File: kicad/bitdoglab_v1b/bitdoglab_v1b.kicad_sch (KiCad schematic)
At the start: 35 parts, among them J1 WS2812, J10 Conn_01x05_Pin, J11 Conn_02x05_Counter_Clockwise, J2 conector_idc, J3 JOYSTICK, J4 jumper_mic, J5 Conn_01x05_Pin, J6 Conn_01x05_Pin, J8 Conn_02x05_Counter_Clockwise, J9 Conn_01x05_Pin, Q1 BC337, Q2 BC337, Q3 DMG2305UX-13, SW1 RESET, SW2 Button_A, SW3 Button_B, U1 uA7805, U2 1063, U3 Charger2A

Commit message: Começo da construção do layout
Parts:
- removed J11, J8: Conn_02x05_Counter_Clockwise, symbol Connector_Generic:Conn_02x05_Counter_Clockwise
- added J13: GP03, Connector_Wire:SolderWire-2sqmm_1x02_P7.8mm_D2mm_OD3.9mm, symbol Connector_Generic:Conn_01x01
- added J14: GP02, Connector_Wire:SolderWire-2sqmm_1x02_P7.8mm_D2mm_OD3.9mm, symbol Connector_Generic:Conn_01x01
- added J15: GP01, Connector_Wire:SolderWire-2sqmm_1x02_P7.8mm_D2mm_OD3.9mm, symbol Connector_Generic:Conn_01x01
- added J16: GP00, Connector_Wire:SolderWire-2sqmm_1x02_P7.8mm_D2mm_OD3.9mm, symbol Connector_Generic:Conn_01x01
- added J5: GND, Connector_Wire:SolderWire-2sqmm_1x02_P7.8mm_D2mm_OD3.9mm, symbol Connector_Generic:Conn_01x01
- added J6: GP28, Connector_Wire:SolderWire-2sqmm_1x02_P7.8mm_D2mm_OD3.9mm, symbol Connector_Generic:Conn_01x01
- added J7: AGND, Connector_Wire:SolderWire-2sqmm_1x02_P7.8mm_D2mm_OD3.9mm, symbol Connector_Generic:Conn_01x01
- added J8: 3.3_OUT, Connector_Wire:SolderWire-2sqmm_1x02_P7.8mm_D2mm_OD3.9mm, symbol Connector_Generic:Conn_01x01
- added J9: VBUS, Connector_Wire:SolderWire-2sqmm_1x02_P7.8mm_D2mm_OD3.9mm, symbol Connector_Generic:Conn_01x01
- added U1: 3.3v_tht, Package_TO_SOT_THT:TO-220-3_Vertical, symbol dk_PMIC-Voltage-Regulators-Linear:LD1117V33
- A1: footprint Raspberry_Pi_Pico_W_Kicad_Files-main:MODULE_SC0918 -> user_Raspberry_Pi_Pico_W_Kicad_Files-main:MODULE_SC0918
- BT1: footprint (none) -> Battery:BatteryHolder_MPD_BH-18650-PC2
- BZ2: renamed from BZ3; footprint (none) -> Buzzer_Beeper:MagneticBuzzer_CUI_CMT-8504-100-SMT
- BZ4: footprint (none) -> Buzzer_Beeper:MagneticBuzzer_CUI_CMT-8504-100-SMT
- C1, C2: footprint (none) -> Capacitor_SMD:CP_Elec_5x5.9
- D1: footprint (none) -> LED_SMD:LED_RGB_5050-6
- D2: footprint (none) -> LED_THT:LED_D5.0mm-4_RGB_Wide_Pins
- J1: renamed from J2; footprint (none) -> Connector_PinHeader_2.54mm:PinHeader_2x07_P2.54mm_Vertical
- J10: renamed from J5; footprint (none) -> Connector_PinHeader_2.54mm:PinHeader_1x05_P2.54mm_Vertical
- J11: renamed from J10; footprint (none) -> Connector_PinHeader_2.54mm:PinHeader_1x05_P2.54mm_Vertical
- J12: renamed from J1; value WS2812 -> WS2812 5x5 Matrix led; footprint (none) -> matrix5x5:Ws2812_led_5050_rgb_5x5
- J17: renamed from J3; footprint (none) -> user_ky-023-joystick-module-1.snapshot.4:ky-023
- J2: renamed from J4; footprint (none) -> Connector_PinHeader_2.54mm:PinHeader_1x02_P2.54mm_Vertical
- J3: renamed from J9; footprint (none) -> Connector_PinHeader_2.54mm:PinHeader_1x05_P2.54mm_Vertical
- J4: renamed from J6; footprint (none) -> Connector_PinHeader_2.54mm:PinHeader_1x05_P2.54mm_Vertical
- OLED1: footprint (none) -> user_SSD1306:128x64OLED
- Q1: renamed from Q3; footprint digikey-footprints:SOT-23-3 -> Package_TO_SOT_SMD:SOT-23-3
- Q2: renamed from Q1; footprint Package_TO_SOT_THT:TO-92_Inline -> Package_TO_SOT_THT:TO-92
- Q3: renamed from Q2; footprint Package_TO_SOT_THT:TO-92_Inline -> Package_TO_SOT_THT:TO-92
- R1: renamed from R4; value R -> 330; footprint (none) -> Resistor_THT:R_Axial_DIN0207_L6.3mm_D2.5mm_P7.62mm_Horizontal
- R2: renamed from R1; value R -> 330; footprint (none) -> Resistor_THT:R_Axial_DIN0207_L6.3mm_D2.5mm_P7.62mm_Horizontal
- Rb1: renamed from Rb; footprint (none) -> Resistor_THT:R_Axial_DIN0207_L6.3mm_D2.5mm_P7.62mm_Horizontal
- Rg1: renamed from Rg; footprint (none) -> Resistor_THT:R_Axial_DIN0207_L6.3mm_D2.5mm_P7.62mm_Horizontal
- Rr1: renamed from Rr; footprint (none) -> Resistor_THT:R_Axial_DIN0207_L6.3mm_D2.5mm_P7.62mm_Horizontal
- SW1, SW2, SW3: footprint (none) -> Button_Switch_THT:SW_PUSH_6mm
- U2: renamed from U1; value uA7805 -> 3.3v_smd; footprint (none) -> Package_TO_SOT_SMD:SOT-223
- U3: value Charger2A -> BAT (DIS)CHARGE; footprint (none) -> user_HW775-main:Charger2A
- U4: renamed from U2; footprint MODULE_1063 -> user_SSD1306:128x64OLED
- renumbered BZ2 to BZ3
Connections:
- net +3.3V: now also U1.2
- net 3.3_OUT: no longer J4.3 (Pin_3)
- net GNDREF: now also J5.1 (Pin_1), U1.1; no longer J4.4 (Pin_4)
- net GP0: no longer J11.4 (Pin_4)
- net GP01: no longer J11.3 (Pin_3)
- net GP02: no longer J11.2 (Pin_2)
- net GP03: no longer J11.1 (Pin_1)
- net VBUS: now also U1.3; no longer J4.2 (Pin_2)
- net 5 renamed GP28
- net GP28: no longer J4.5 (Pin_5)
- new net 3.3_OUT_EXT: J4.4 (Pin_4), J8.1 (Pin_1)
- new net AGND_EXT: J4.3 (Pin_3), J7.1 (Pin_1)
- new net GP01_EXT: J11.3 (Pin_3), J15.1 (Pin_1)
- new net GP02_EXT: J11.2 (Pin_2), J14.1 (Pin_1)
- new net GP03_EXT: J11.1 (Pin_1), J13.1 (Pin_1)
- new net GP0_EXT: J11.4 (Pin_4), J16.1 (Pin_1)
- new net GP28_EXT: J4.2 (Pin_2), J6.1 (Pin_1)
- new net VBUS_EXT: J4.5 (Pin_5), J9.1 (Pin_1)
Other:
- moved on the sheet: C1, C2

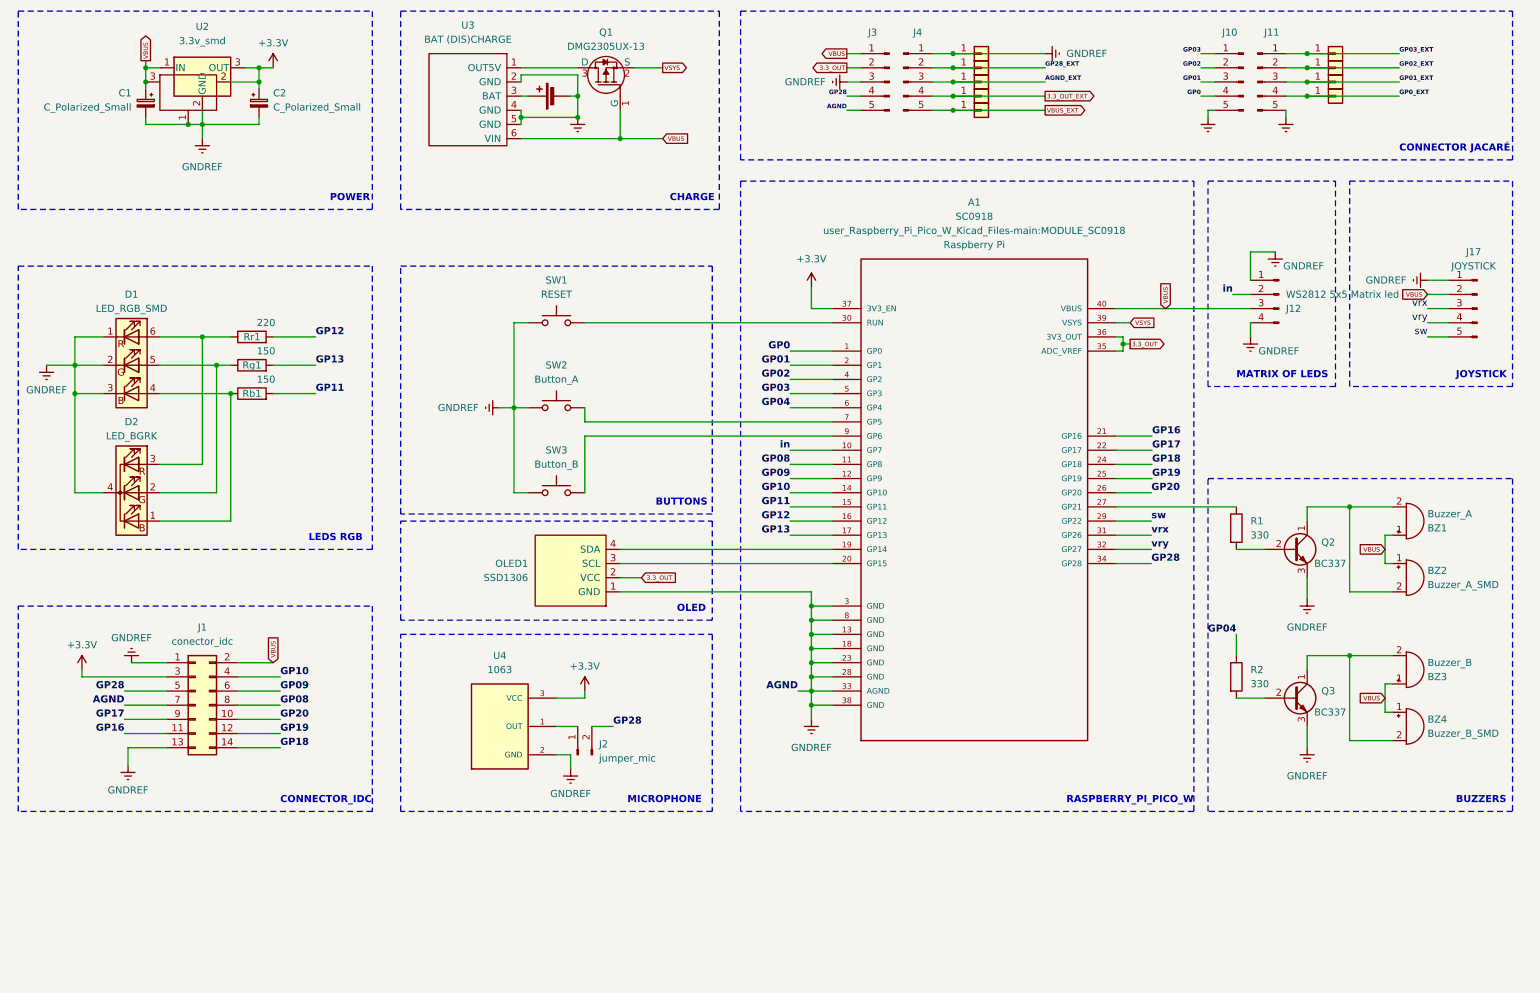
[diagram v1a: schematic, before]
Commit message: Finalizacao do placement dos componentes
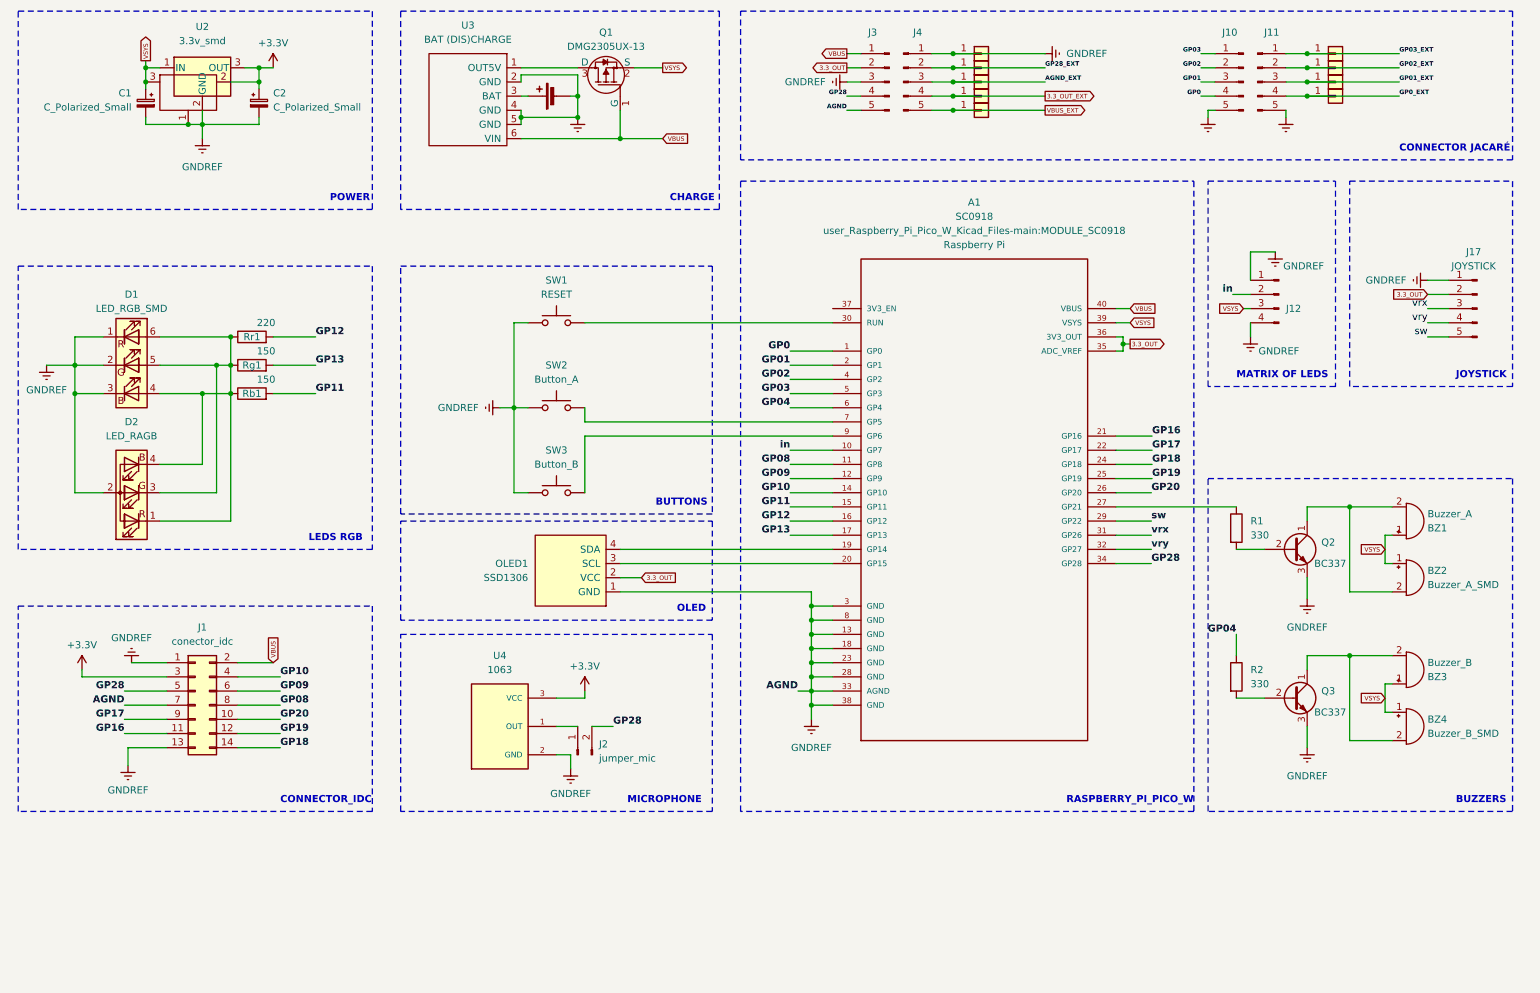
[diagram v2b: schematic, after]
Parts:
- removed D2: LED_BGRK, LED_THT:LED_D5.0mm-4_RGB_Wide_Pins, symbol Device:LED_BGRK
- added D2: LED_RAGB, LED_THT:LED_D5.0mm-4_RGB_Wide_Pins, symbol Device:LED_RAGB
- J12: value WS2812 5x5 Matrix led -> 5x5 Matrix led
- U4: footprint user_SSD1306:128x64OLED -> user_1063:MODULE_1063
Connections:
- net +3.3V: no longer A1.37 (3V3_EN)
- net 3.3_OUT: now also J17.2 (Pin_2)
- net GNDREF: now also SW1.2, SW2.2, SW3.2, D2.2 (A); no longer SW1.1, SW2.1, SW3.1
- net VBUS: no longer BZ1.1 (-), BZ2.1 (-), BZ3.1 (-), BZ4.1 (-), C1.1, J12.3 (Pin_3), J17.2 (Pin_2), U1.3, U2.1 (IN)
- net VSYS: now also BZ1.1 (-), BZ2.1 (-), BZ3.1 (-), BZ4.1 (-), C1.1, J12.3 (Pin_3), U1.3, U2.1 (IN)
- net at D1.5 (GA), Rg1.1: now also D1.4 (BA), D1.6 (RA), Rb1.1, Rr1.1, D2.1 (RK), D2.3 (GK), D2.4 (BK)
- net at A1.30 (RUN): now also SW1.1; no longer SW1.2
- net at A1.7 (GP5): now also SW2.1; no longer SW2.2
- net at A1.9 (GP6): now also SW3.1; no longer SW3.2

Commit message: roteamento e apagando backups
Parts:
- added J1, J3: Conn_01x20_Socket, Connector_PinHeader_2.54mm:PinHeader_1x20_P2.54mm_Vertical, symbol Connector:Conn_01x20_Socket
- renumbered J8 to J10, J9 to J11, J10 to J12, J11 to J13, J12 to J14, J13 to J15, J14 to J16, J15 to J17, J16 to J18, J17 to J19, J1 to J2, J2 to J4, J3 to J5, J4 to J6, J5 to J7, J6 to J8, J7 to J9
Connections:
- net 3.3_OUT: now also J3.15 (Pin_15), J3.16 (Pin_16)
- net GNDREF: now also J1.13 (Pin_13), J1.18 (Pin_18), J1.3 (Pin_3), J1.8 (Pin_8), J3.13 (Pin_13), J3.18 (Pin_18), J3.3 (Pin_3), J3.8 (Pin_8)
- net GP0: now also J1.1 (Pin_1)
- net GP01: now also J1.2 (Pin_2)
- net GP02: now also J1.4 (Pin_4)
- net GP03: now also J1.5 (Pin_5)
- net GP04: now also J1.6 (Pin_6)
- net GP08: now also J1.11 (Pin_11)
- net GP09: now also J1.12 (Pin_12)
- net GP10: now also J1.14 (Pin_14)
- net GP11: now also J1.15 (Pin_15)
- net GP12: now also J1.16 (Pin_16)
- net GP13: now also J1.17 (Pin_17)
- net GP16: now also J3.1 (Pin_1)
- net GP17: now also J3.2 (Pin_2)
- net GP18: now also J3.4 (Pin_4)
- net GP19: now also J3.5 (Pin_5)
- net GP20: now also J3.6 (Pin_6)
- net GP28: now also J3.14 (Pin_14)
- net VBUS: now also J3.20 (Pin_20)
- net VSYS: now also J3.19 (Pin_19)
- net in: now also J1.10 (Pin_10)
- net pino_27: now reaches A1.27 (GP21), R1.1
- net pino_27: now also J3.7 (Pin_7)
- net pino_19: now reaches A1.19 (GP14), OLED1.4 (SDA)
- net pino_19: now also J1.19 (Pin_19)
- net pino_20: now reaches A1.20 (GP15), OLED1.3 (SCL)
- net pino_20: now also J1.20 (Pin_20)
- net pino_30: now reaches A1.30 (RUN), SW1.1
- net pino_30: now also J3.10 (Pin_10)
- net pino_37: now reaches A1.37 (3V3_EN)
- net pino_37: now also J3.17 (Pin_17)
- net pino_07: now reaches A1.7 (GP5), SW2.1
- net pino_07: now also J1.7 (Pin_7)
- net pino_09: now reaches A1.9 (GP6), SW3.1
- net pino_09: now also J1.9 (Pin_9)
- net sw renamed pino_29
- net pino_29: now also J3.9 (Pin_9)
- net vrx renamed pino_31
- net pino_31: now also J3.11 (Pin_11)
- net vry renamed pino_32
- net pino_32: now also J3.12 (Pin_12)

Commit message: Ajustes no roteamento
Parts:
- removed J10: 3.3_OUT, Connector_Wire:SolderWire-2sqmm_1x02_P7.8mm_D2mm_OD3.9mm, symbol Connector_Generic:Conn_01x01
- removed J11: VBUS, Connector_Wire:SolderWire-2sqmm_1x02_P7.8mm_D2mm_OD3.9mm, symbol Connector_Generic:Conn_01x01
- removed J15: GP03, Connector_Wire:SolderWire-2sqmm_1x02_P7.8mm_D2mm_OD3.9mm, symbol Connector_Generic:Conn_01x01
- removed J16: GP02, Connector_Wire:SolderWire-2sqmm_1x02_P7.8mm_D2mm_OD3.9mm, symbol Connector_Generic:Conn_01x01
- removed J17: GP01, Connector_Wire:SolderWire-2sqmm_1x02_P7.8mm_D2mm_OD3.9mm, symbol Connector_Generic:Conn_01x01
- removed J18: GP00, Connector_Wire:SolderWire-2sqmm_1x02_P7.8mm_D2mm_OD3.9mm, symbol Connector_Generic:Conn_01x01
- removed J8: GP28, Connector_Wire:SolderWire-2sqmm_1x02_P7.8mm_D2mm_OD3.9mm, symbol Connector_Generic:Conn_01x01
- removed J9: AGND, Connector_Wire:SolderWire-2sqmm_1x02_P7.8mm_D2mm_OD3.9mm, symbol Connector_Generic:Conn_01x01
- added J10, J11, J15, J16, J17, J18, J8, J9: GND, Connector_Wire:SolderWire-2sqmm_1x02_P7.8mm_D2mm_OD3.9mm, symbol Connector_custom:Conn_01x02
- D2: symbol Device:LED_RAGB -> Device:LED_RKBG
- J7: symbol Connector_Generic:Conn_01x01 -> Connector_custom:Conn_01x02
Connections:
- net 3.3_OUT_EXT: now also J10.1 (Pin_1), J10.2 (Pin_2)
- net AGND_EXT: now also J9.1 (Pin_1), J9.2 (Pin_2)
- net GNDREF: now also J7.2 (Pin_2)
- net GP01_EXT: now also J17.1 (Pin_1), J17.2 (Pin_2)
- net GP02_EXT: now also J16.1 (Pin_1), J16.2 (Pin_2)
- net GP03_EXT: now also J15.1 (Pin_1), J15.2 (Pin_2)
- net GP0_EXT: now also J18.1 (Pin_1), J18.2 (Pin_2)
- net GP28_EXT: now also J8.1 (Pin_1), J8.2 (Pin_2)
- net VBUS_EXT: now also J11.1 (Pin_1), J11.2 (Pin_2)
- new net: D1.6 (RA), D2.1 (RA), Rr1.1
- new net: D1.4 (BA), D2.3 (BA), Rb1.1
- new net: D1.5 (GA), D2.4 (GA), Rg1.1
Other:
- moved on the sheet: D2
